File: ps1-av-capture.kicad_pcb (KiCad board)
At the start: 4 copper layers, 100 x 80 mm, 237 parts, among them J1 AV_PIGTAIL, J2 USB3_B, J3 USB_C_AUDIO, J4 JTAG, J5 UART, SW1 RESET, U1 TVP7002PZP, U10 TLV75733PDBVR, U11 TLV75533PDBVR, U12 PCM2903CDBR, U2 CYUSB3014-BZXI, U3 24LC1025-I/SN, U4 24LC1025-I/SN, U5 TPS563201DDCR, U6 TPS563201DDCR, U7 TPS563201DDCR, U8 TLV75519PDBVR, U9 TLV75519PDBVR, X1 27MHz, Y1 19.2MHz, Y2 12MHz

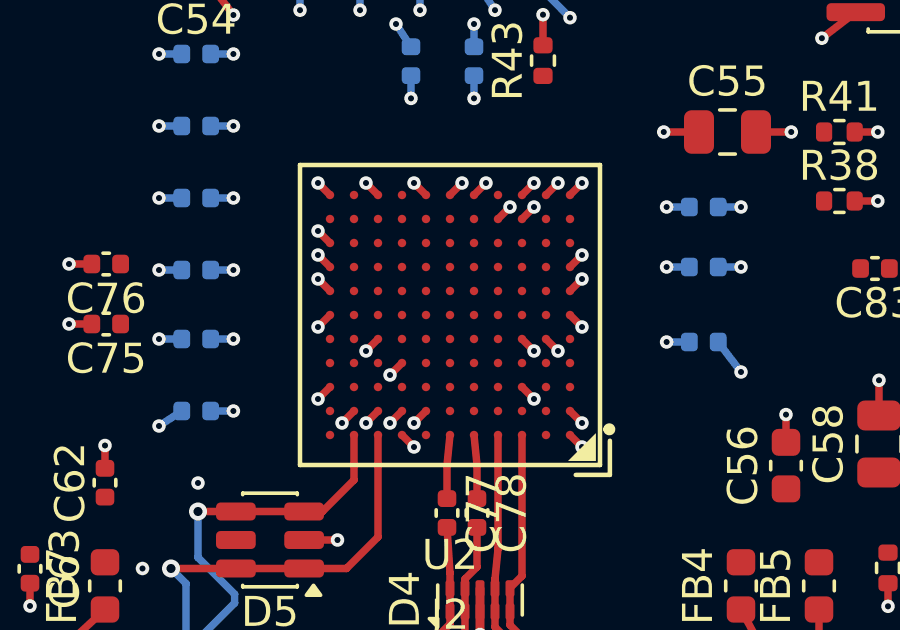
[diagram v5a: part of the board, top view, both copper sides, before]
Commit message: Layout: FX3 escape phase 1, dogbone vias for the inner signal balls
tools/escape.py gives every U2 signal ball from ring 3 inward (27 balls) a
dogbone via in a free diagonal cell, preferring the cell that points towards
U1 for the GPIF/TVP nets. Rings 1 and 2 will escape on L1. The vias dangle
until the escape routes land.
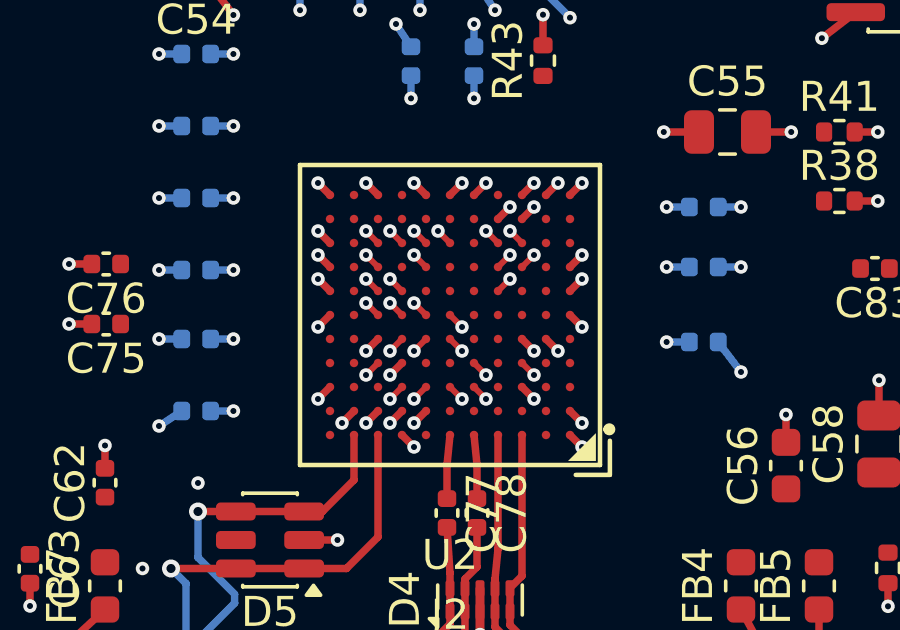
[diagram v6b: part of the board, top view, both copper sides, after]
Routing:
- net VD_SOG: track 0.00 -> 0.57 mm, vias 0 -> 1
- net VD_G9: track 0.00 -> 0.57 mm, vias 0 -> 1
- net VD_FID: track 0.00 -> 0.57 mm, vias 0 -> 1
- net VD_B6: track 0.00 -> 0.57 mm, vias 0 -> 1
- net VD_B4: track 0.00 -> 0.57 mm, vias 0 -> 1
- net FX3_XO: track 0.00 -> 0.57 mm, vias 0 -> 1
- net FX3_PMODE0: track 0.00 -> 0.57 mm, vias 0 -> 1
- net FX3_TDI: track 0.00 -> 0.57 mm, vias 0 -> 1
- net VD_R9: track 0.00 -> 0.57 mm, vias 0 -> 1
- net VD_R6: track 0.00 -> 0.57 mm, vias 0 -> 1
- net VD_R3: track 0.00 -> 0.57 mm, vias 0 -> 1
- net VD_PCLK: track 0.00 -> 0.57 mm, vias 0 -> 1
- net VD_G8: track 0.00 -> 0.57 mm, vias 0 -> 1
- net VD_G3: track 0.00 -> 0.57 mm, vias 0 -> 1
- net VD_B9: track 0.00 -> 0.57 mm, vias 0 -> 1
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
